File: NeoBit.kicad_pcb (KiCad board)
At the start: 2 copper layers, 67.3 x 35.6 mm, 26 parts, among them J1 Feather_Long, J2 Barrel_Jack_MountingPin, J3 Feather_Short, J4 NeoPixels, J5 microbit_edge_connector, U1 74AHCT125, U2 MCP1702-3302E_TO92

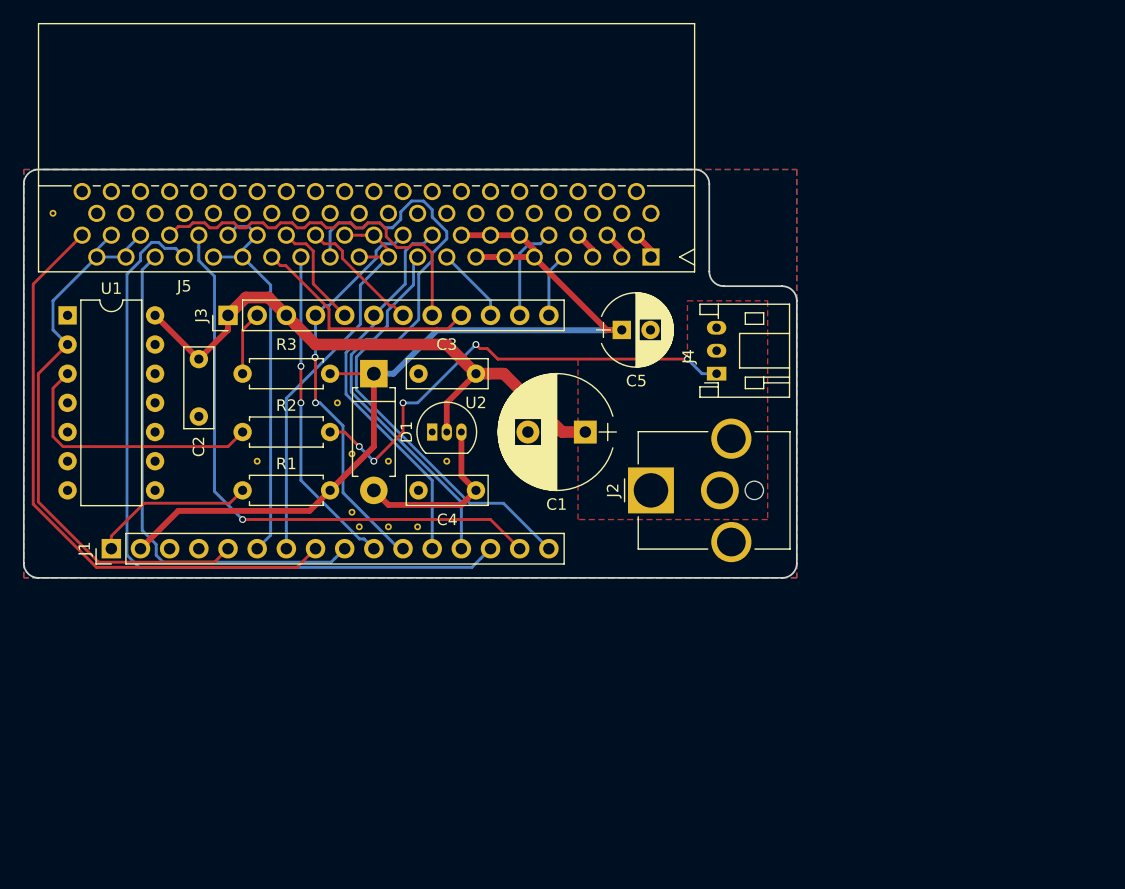
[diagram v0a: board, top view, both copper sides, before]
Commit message: Remove old components and tracks.
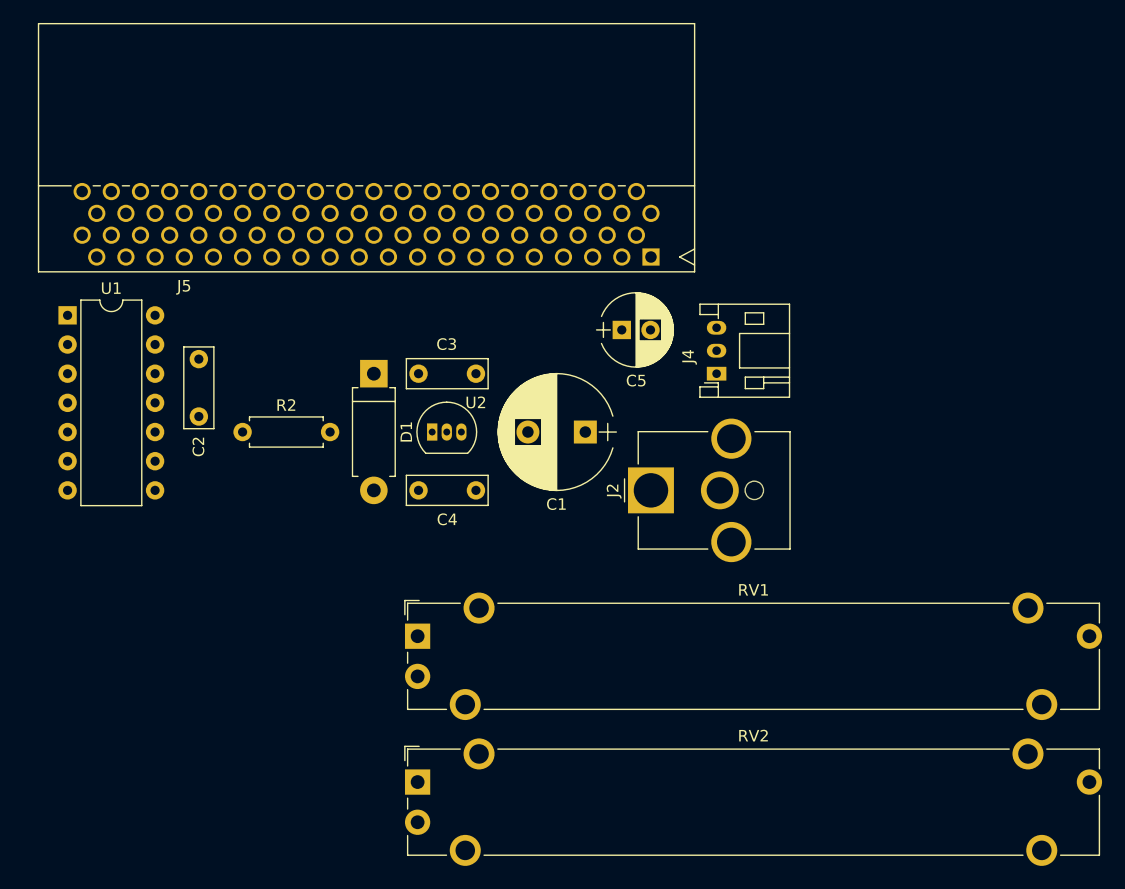
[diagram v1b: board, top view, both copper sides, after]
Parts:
- removed J1: Feather_Long, Socket_Strips:Socket_Strip_Straight_1x16_Pitch2.54mm
- removed J3: Feather_Short, Socket_Strips:Socket_Strip_Straight_1x12_Pitch2.54mm
- removed R1, R3: 10K, Resistors_THT:R_Axial_DIN0207_L6.3mm_D2.5mm_P7.62mm_Horizontal
- removed VIA (x10): VIA-0.6mm, footprints:VIA-0.6mm
- added RV1: 10K, footprints:Bourns_PTA4543, F.Cu at (152.4, 124.5)
- added RV2: 10K, footprints:Bourns_PTA4543, F.Cu at (152.4, 137.2)
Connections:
- J5 pad 13: /SDA -> Net-(J5-Pad13)
- J5 pad 15: /SCL -> Net-(J5-Pad15)
- J5 pad 29: /P16 -> Net-(J5-Pad29)
- J5 pad 31: /MOSI -> Net-(J5-Pad31)
- J5 pad 33: /MISO -> Net-(J5-Pad33)
- J5 pad 35: /SCK -> Net-(J5-Pad35)
- J5 pad 45: /P12 -> Net-(J5-Pad45)
- J5 pad 47: /P11 -> Net-(J5-Pad47)
- J5 pad 49: /P10 -> Net-(J5-Pad49)
- J5 pad 51: /P9 -> Net-(J5-Pad51)
- J5 pad 53: /P8 -> Net-(J5-Pad53)
- J5 pad 63: /P7 -> Net-(J5-Pad63)
- J5 pad 65: /P6 -> Net-(J5-Pad65)
- J5 pad 67: /P5 -> Net-(J5-Pad67)
- J5 pad 69: /P4 -> Net-(J5-Pad69)
- J5 pad 79: /P3 -> Net-(J5-Pad79)
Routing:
- net +3V3: track 80.2 -> 0.00 mm
- net /P6: track 64.3 -> 0.00 mm
- net /P12: track 56.9 -> 0.00 mm
- net +5V: track 53.0 -> 0.00 mm
- net /P3: track 52.7 -> 0.00 mm
- net /P7: track 51.5 -> 0.00 mm, vias 1 -> 0
- net /P0: track 51.1 -> 0.00 mm
- net /P4: track 44.1 -> 0.00 mm
- net Net-(J4-Pad1): track 41.5 -> 0.00 mm, vias 5 -> 0
- net /P2: track 36.6 -> 0.00 mm
- net /P1: track 35.0 -> 0.00 mm
- net /SCK: track 34.8 -> 0.00 mm, vias 2 -> 0
- net /MOSI: track 34.1 -> 0.00 mm
- net /P5: track 32.6 -> 0.00 mm
- net /MISO: track 32.1 -> 0.00 mm
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- removed copper zone on F.Cu, net +5V
- removed copper zone on B.Cu, net GND
- removed copper zone on F.Cu, net GND
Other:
- board outline removed

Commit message: Footprints are mostly positioned.
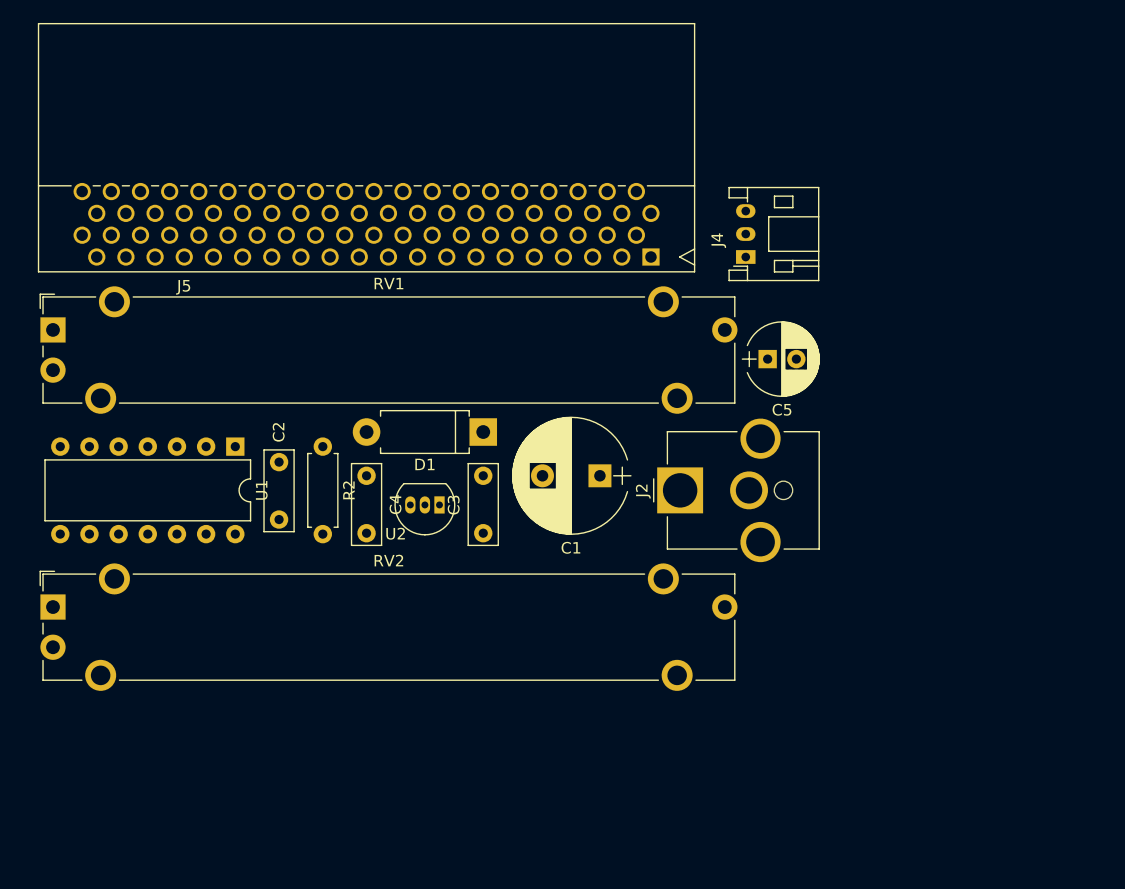
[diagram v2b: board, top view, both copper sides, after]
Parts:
- moved RV1 41.5 mm to (120.7, 97.8)
- moved RV2 35.2 mm to (120.7, 121.9)
- moved U1 18.5 mm to (136.5, 108.0), turned to 270 degrees
- moved C2 15.6 mm to (140.3, 114.3), turned to 90 degrees
- moved C5 13.0 mm to (182.9, 100.3)
- moved D1 10.8 mm to (158.1, 106.7), turned to 180 degrees
- moved J4 10.5 mm to (181.0, 91.4)
- moved C4 9.61 mm to (148.0, 110.5), turned to 270 degrees
- moved C3 8.91 mm to (158.1, 110.5), turned to 270 degrees
- moved R2 7.10 mm to (144.1, 108.0), turned to 270 degrees
- moved U2 6.38 mm to (154.3, 113.0), turned to 180 degrees
- moved C1 4.02 mm to (168.3, 110.5)
- moved J2 2.54 mm to (175.3, 111.8)

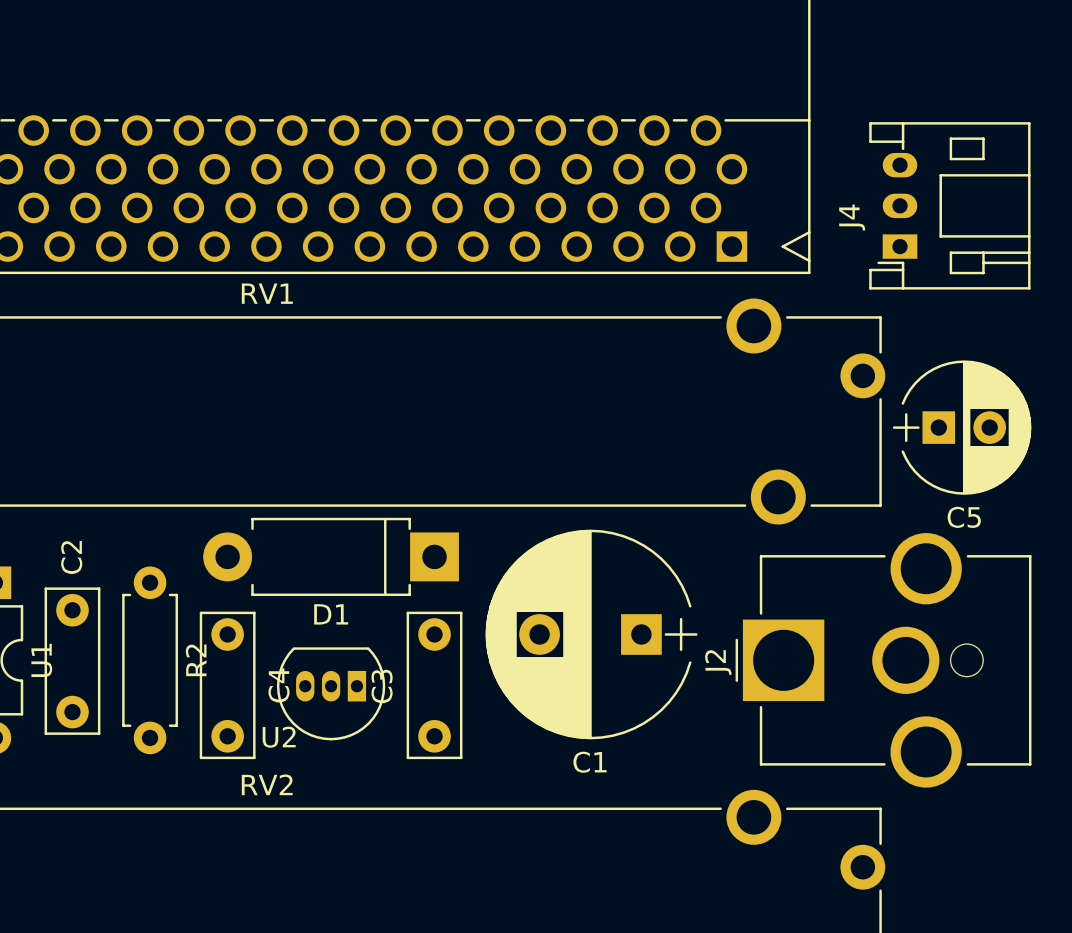
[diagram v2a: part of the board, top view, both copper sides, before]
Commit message: Adjust footprint placement.
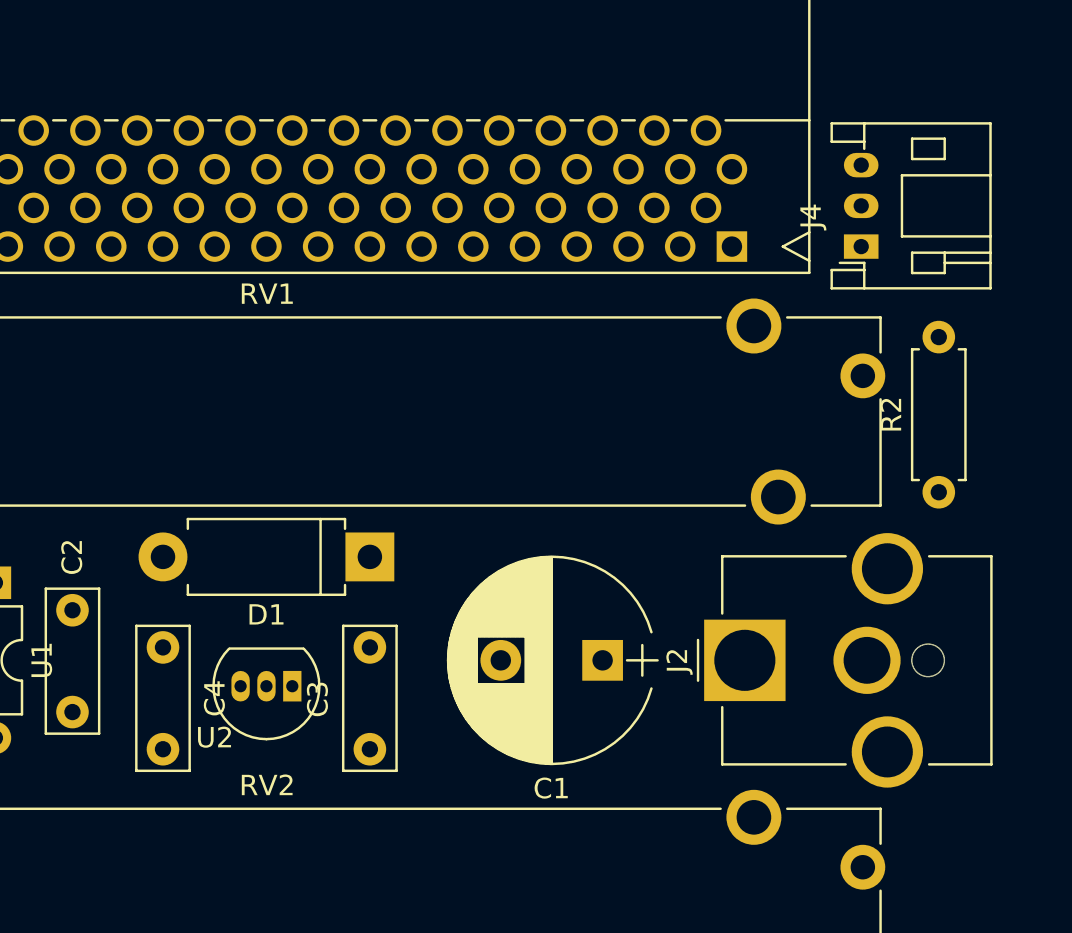
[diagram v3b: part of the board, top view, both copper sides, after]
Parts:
- removed C5: 47µF, Capacitors_THT:CP_Radial_D6.3mm_P2.50mm
- moved R2 39.0 mm to (182.9, 103.5), turned to 90 degrees
- moved C3 3.24 mm to (154.9, 111.1)
- moved C4 3.24 mm to (144.8, 111.1)
- moved D1 3.18 mm to (154.9, 106.7)
- moved U2 3.18 mm to (151.1, 113.0)
- moved C1 2.29 mm to (166.4, 111.8)
- moved J2 1.91 mm to (173.4, 111.8)
- moved J4 1.91 mm to (179.1, 91.4)

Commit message: Draw board outline.
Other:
- board outline added: 67.3 x 45.7 mm
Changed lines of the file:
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@@
     (area 0 0 0 0)
     (thickness 1.6)
-    (drawings 0)
+    (drawings 8)
     (tracks 0)
     (zones 0)
@@
     (pad_to_mask_clearance 0)
     (aux_axis_origin 0 0)
-    (visible_elements FFFEE77F)
+    (visible_elements FFFEF77F)
     (pcbplotparams
       (layerselection 0x00030_80000001)
@@
     )
   )
+  (gr_line (start 183.515 83.82) (end 121.285 83.82) (angle 90) (layer Edge.Cuts) (width 0.15))
+  (gr_line (start 186.055 127) (end 186.055 86.36) (angle 90) (layer Edge.Cuts) (width 0.15))
+  (gr_line (start 121.285 129.54) (end 183.515 129.54) (angle 90) (layer Edge.Cuts) (width 0.15))
+  (gr_line (start 118.745 86.36) (end 118.745 127) (angle 90) (layer Edge.Cuts) (width 0.15))
+  (gr_arc (start 183.515 127) (end 186.055 127) (angle 90) (layer Edge.Cuts) (width 0.15))
+  (gr_arc (start 183.515 86.36) (end 183.515 83.82) (angle 90) (layer Edge.Cuts) (width 0.15))
+  (gr_arc (start 121.285 127) (end 121.285 129.54) (angle 90) (layer Edge.Cuts) (width 0.15))
+  (gr_arc (start 121.285 86.36) (end 118.745 86.36) (angle 90) (layer Edge.Cuts) (width 0.15))
 )

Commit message: Position text.
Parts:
- moved D1 0.63 mm to (154.9, 107.3)
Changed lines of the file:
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@@
     (descr "C, Rect series, Radial, pin pitch=5.00mm, , length*width=7*2.5mm^2, Capacitor")
     (tags "C Rect series Radial pin pitch 5.00mm  length 7mm width 2.5mm Capacitor")
-    (fp_text reference C3 (at 2.54 2.54 270) (layer F.SilkS)
+    (fp_text reference C3 (at 2.54 -2.54 270) (layer F.SilkS)
       (effects (font (size 1 1) (thickness 0.15)))
     )
@@
     (descr "C, Rect series, Radial, pin pitch=5.00mm, , length*width=7*2.5mm^2, Capacitor")
     (tags "C Rect series Radial pin pitch 5.00mm  length 7mm width 2.5mm Capacitor")
-    (fp_text reference C4 (at 2.5 -2.56 270) (layer F.SilkS)
+    (fp_text reference C4 (at -0.635 -2.54 270) (layer F.SilkS)
       (effects (font (size 1 1) (thickness 0.15)))
     )
@@
   )
   (module Diodes_THT:D_DO-15_P10.16mm_Horizontal (layer F.Cu)
-    (at 154.94 106.68 180)
+    (at 154.94 107.315 180)
     (descr "D, DO-15 series, Axial, Horizontal, pin pitch=10.16mm, , length*diameter=7.6*3.6mm^2, , http://www.diodes.com/_files/packages/DO-15.pdf")
     (tags "D DO-15 series Axial Horizontal pin pitch 10.16mm  length 7.6mm diameter 3.6mm")
@@
     (descr "JST PH series connector, S3B-PH-K, side entry type, through hole, Datasheet: http://www.jst-mfg.com/product/pdf/eng/ePH.pdf")
     (tags "connector jst ph")
-    (fp_text reference J4 (at 1.5 -2.45 90) (layer F.SilkS)
+    (fp_text reference J4 (at -3.175 5.715 90) (layer F.SilkS)
       (effects (font (size 1 1) (thickness 0.15)))
     )
@@
     (descr "Resistor, Axial_DIN0207 series, Axial, Horizontal, pin pitch=7.62mm, 0.25W = 1/4W, length*diameter=6.3*2.5mm^2, http://cdn-reichelt.de/documents/datenblatt/B400/1_4W%23YAG.pdf")
     (tags "Resistor Axial_DIN0207 series Axial Horizontal pin pitch 7.62mm 0.25W = 1/4W length 6.3mm diameter 2.5mm")
-    (fp_text reference R2 (at 3.81 -2.31 90) (layer F.SilkS)
+    (fp_text reference R2 (at -0.635 1.905 90) (layer F.SilkS)
       (effects (font (size 1 1) (thickness 0.15)))
     )
@@
     (descr "14-lead though-hole mounted DIP package, row spacing 7.62 mm (300 mils)")
     (tags "THT DIP DIL PDIP 2.54mm 7.62mm 300mil")
-    (fp_text reference U1 (at 3.81 -2.33 270) (layer F.SilkS)
+    (fp_text reference U1 (at 8.89 -1.905 270) (layer F.SilkS)
       (effects (font (size 1 1) (thickness 0.15)))
     )
@@
     (descr "TO-92 leads in-line, narrow, oval pads, drill 0.6mm (see NXP sot054_po.pdf)")
     (tags "to-92 sc-43 sc-43a sot54 PA33 transistor")
-    (fp_text reference U2 (at 3.81 -2.54 180) (layer F.SilkS)
+    (fp_text reference U2 (at 3.175 -3.175 180) (layer F.SilkS)
       (effects (font (size 1 1) (thickness 0.15)))
     )
@@
     (descr "BBC micro:bit right-angle edge connector")
     (tags "bbc microbit edge connector right-angle")
-    (fp_text reference J5 (at 40.64 -2.54 180) (layer F.SilkS)
+    (fp_text reference J5 (at 22.86 -2.54 180) (layer F.SilkS)
       (effects (font (size 1 1) (thickness 0.15)))
     )
@@
     (descr "Bourns single-gang slide potentiometer, 45mm travel")
     (tags "Bourns single-gang slide potentiometer 45mm")
-    (fp_text reference RV1 (at 29.25 -4) (layer F.SilkS)
-      (effects (font (size 1 1) (thickness 0.15)))
-    )
+    (fp_text reference RV1 (at 16.51 7.62) (layer F.SilkS)
+      (effects (font (size 1 1) (thickness 0.15)))
+    )
